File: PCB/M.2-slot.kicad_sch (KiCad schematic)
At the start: 2 parts, among them J1 Bus_M.2_Socket_M

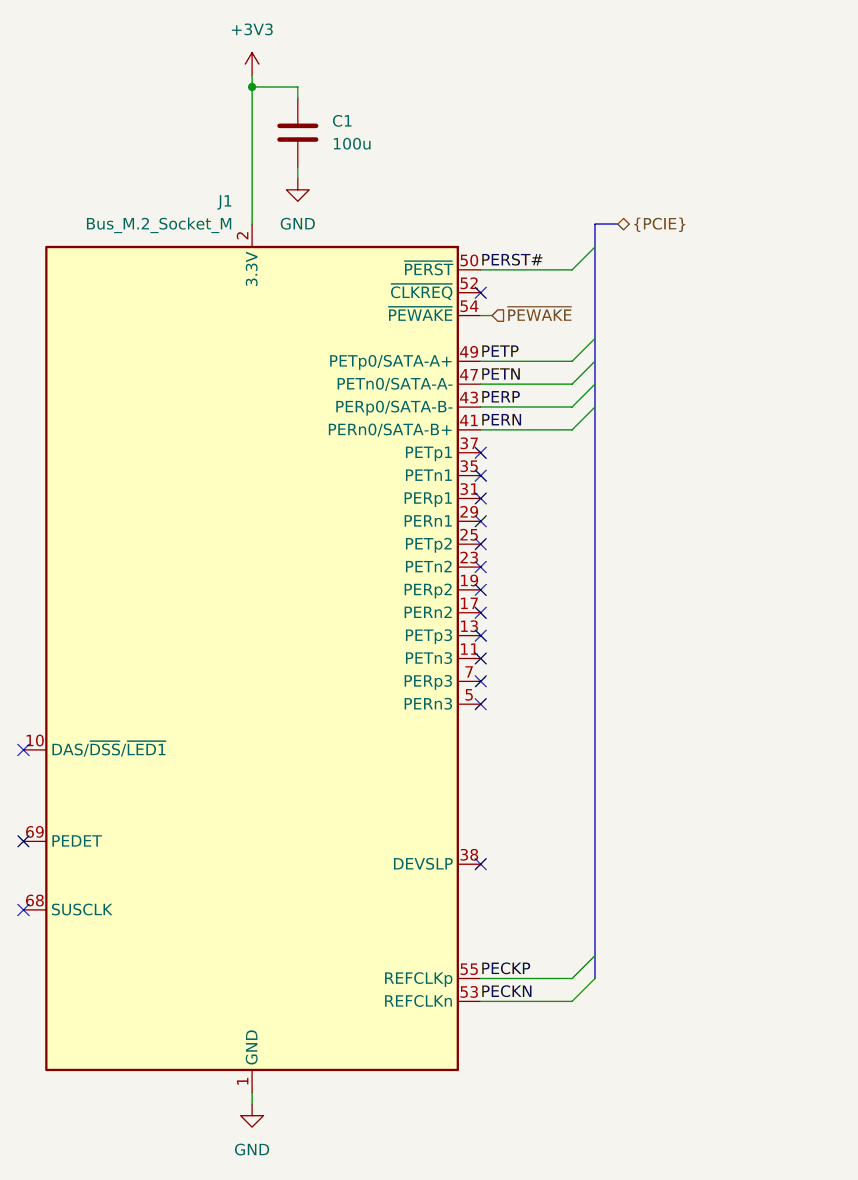
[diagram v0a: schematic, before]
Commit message: Added silkscreen
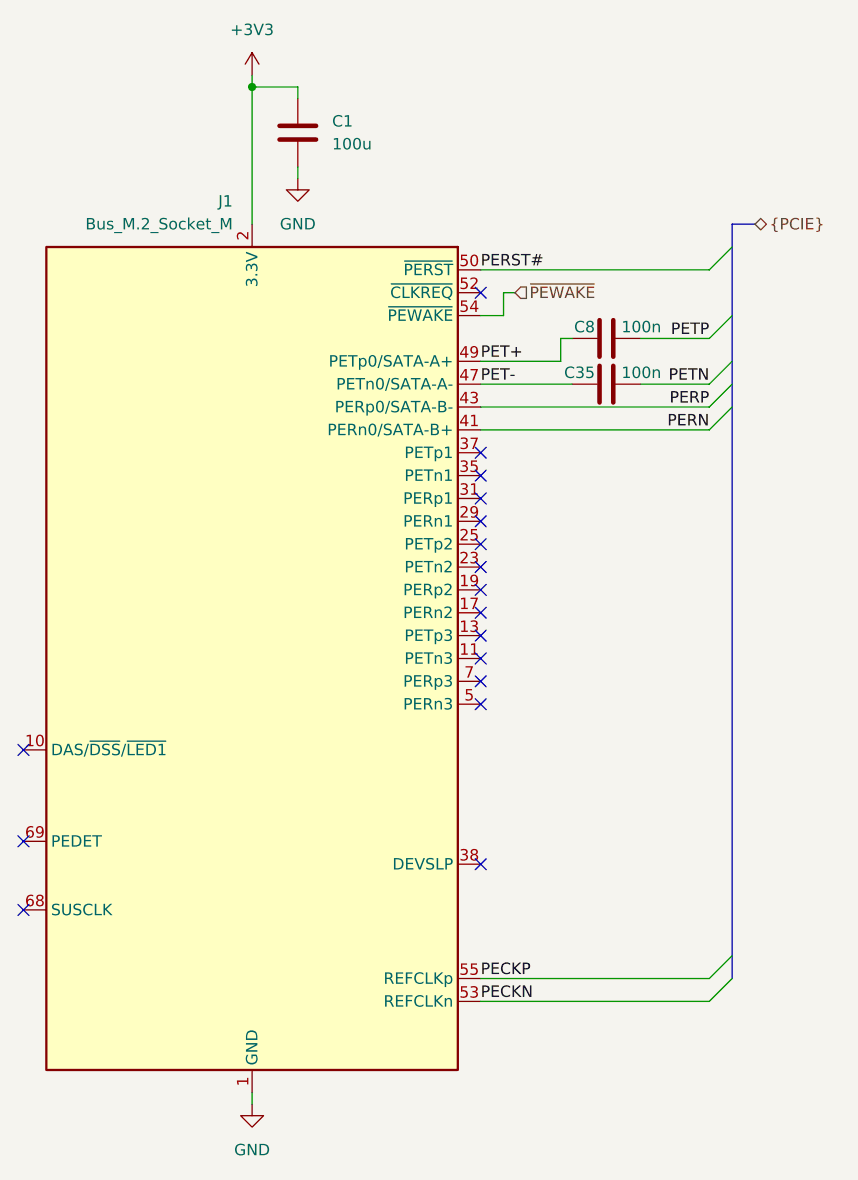
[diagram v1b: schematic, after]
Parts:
- added C35, C8: 100n, Capacitor_SMD:C_0402_1005Metric, symbol Device:C
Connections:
- net PETN: now also C35.2; no longer J1.47 (PETn0/SATA-A-)
- net PETP: now also C8.2; no longer J1.49 (PETp0/SATA-A+)
- new net PET+: C8.1, J1.49 (PETp0/SATA-A+)
- new net PET-: C35.1, J1.47 (PETn0/SATA-A-)
